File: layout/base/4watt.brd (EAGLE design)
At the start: 50 x 50 mm, 45 parts, among them IC2 FT232RL, Q1 IRF7413, Q2 IRF7413, Q3 IRF7413, Q4 IRF7413, T1 BC848, T2 BC848, T3 BC848, T4 BC848, T5 BC848, T6 BC848, U1 MOD-WIFI-ESP8266-DEV_SMD

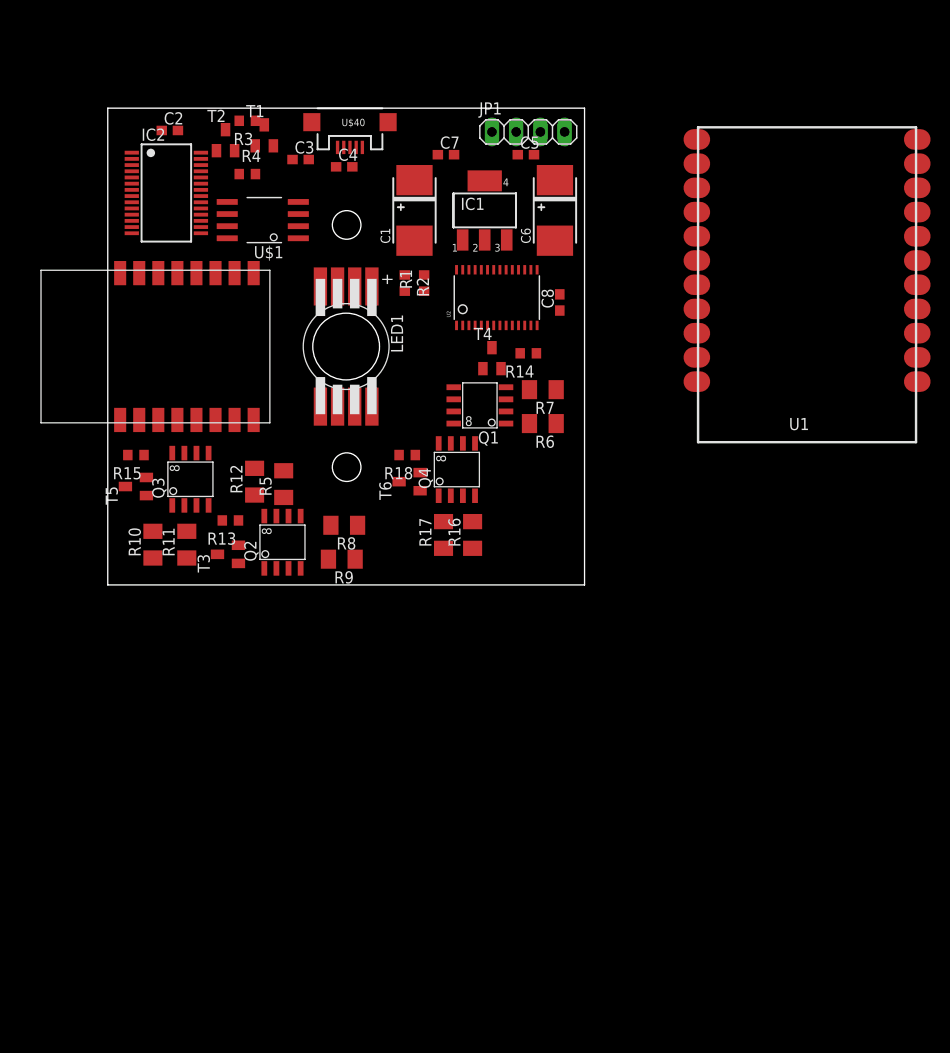
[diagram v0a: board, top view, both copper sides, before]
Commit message: new pinout
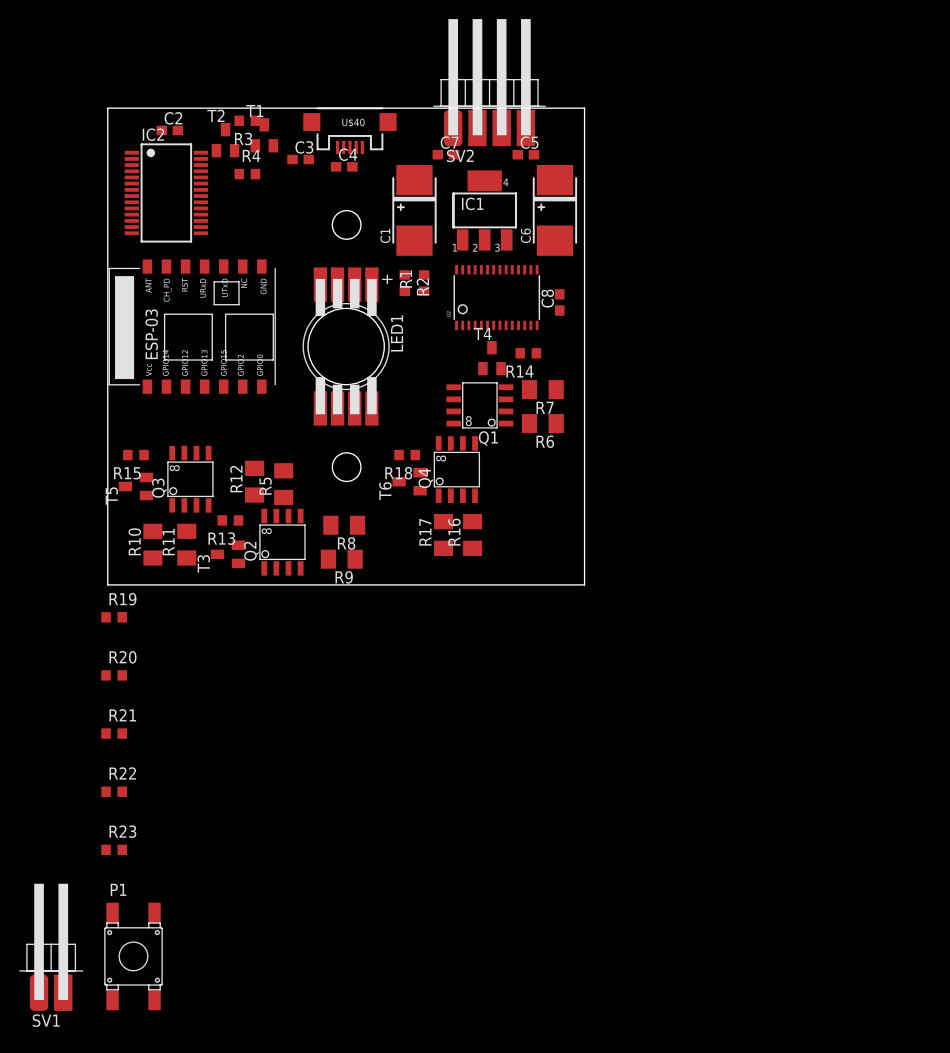
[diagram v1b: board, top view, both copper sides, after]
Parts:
- removed IC3: (no value), ESP8266-2:ESP-12
- removed JP1: (no value), pinhead-2:1X04
- removed U$1: DUMMY, SparkFun:SO08WIDE
- removed U1: MOD-WIFI-ESP8266-DEV_SMD, ESP8266 2:MOD-WIFI-ESP8266-DEV_SMD
- added P1: FSM4JSMA-SMD, switch-misc:FSM4JSMA-SMD
- added R19, R20, R21, R22, R23: 10k, rcl-2:R0603
- added SV1: 1X2SMD-2.54LIEGEND, sid:1X2SMD-2.54LIEGEND
- added SV2: 1X4SMD-2.54LIEGEND, sid:1X4SMD-2.54LIEGEND
- added U$2: ESP8266, ESP8266:ESP-03
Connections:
- removed net GPIO13: U1.18
- removed net VCC: U$1.6
- new net N$2: R19.1, U$2.CH_PD
- new net N$6: R21.1, U$2.GPIO2
- net +3V3: now also R19.2, R20.2, R21.2, R23.2, U$2.VCC; no longer U1.1
- net +5V: now also SV2.P$4
- net GND: now also P1.P$3, P1.P$4, R22.1, SV1.P$1, SV2.P$1, U$2.GND; no longer U$1.7, U1.2
- net GPIO0: now also P1.P$1, P1.P$2, R23.1, SV1.P$2, U$2.GPIO0; no longer U1.21
- net GPIO15: now also R22.2, U$2.GPIO15; no longer U1.19
- net N$3: now also SV2.P$2
- net N$4: now also SV2.P$3
- net RST: now also R20.1, U$2.GPIO18; no longer U1.13
- net RX: now also U$2.URXD
- net SCL: now also U$2.GPIO12; no longer U1.22
- net SDA: now also U$2.NC; no longer U1.11
- net TX: now also U$2.UTXD

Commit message: extclk to gnd
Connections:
- net GND: now also U2.25
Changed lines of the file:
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@@
 <contactref element="SV1" pad="P$1"/>
 <contactref element="SV2" pad="P$1"/>
+<contactref element="U2" pad="25"/>
 <wire x1="46.316" y1="55.118" x2="54.698" y2="55.118" width="0" layer="19" extent="1-1"/>
-<wire x1="39.4" y1="58.532" x2="46.316" y2="55.118" width="0" layer="19" extent="1-1"/>
+<wire x1="46.228" y1="57.912" x2="46.316" y2="55.118" width="0" layer="19" extent="1-1"/>
+<wire x1="39.4" y1="58.532" x2="46.228" y2="57.912" width="0" layer="19" extent="1-1"/>
 <wire x1="34.1" y1="55.882" x2="39.4" y2="58.532" width="0" layer="19" extent="1-1"/>
 <wire x1="35.648" y1="53.848" x2="34.1" y2="55.882" width="0" layer="19" extent="1-1"/>
@@
 <wire x1="31.4" y1="58.532" x2="34.1" y2="55.882" width="0" layer="19" extent="1-1"/>
 <wire x1="47.2191" y1="46.1769" x2="46.316" y2="55.118" width="0" layer="19" extent="1-1"/>
-<wire x1="49.175" y1="43.0498" x2="47.2191" y2="46.1769" width="0" layer="19" extent="1-1"/>
+<wire x1="48.525" y1="43.0498" x2="47.2191" y2="46.1769" width="0" layer="19" extent="1-1"/>
+<wire x1="49.175" y1="43.0498" x2="48.525" y2="43.0498" width="0" layer="19" extent="1-1"/>
 <wire x1="49.825" y1="43.0498" x2="49.175" y2="43.0498" width="0" layer="19" extent="1-1"/>
 <wire x1="42.164" y1="46.101" x2="47.2191" y2="46.1769" width="0" layer="19" extent="1-1"/>
@@
 <wire x1="14.904" y1="-33.556" x2="14.904" y2="-24.372" width="0" layer="19" extent="1-1"/>
 <wire x1="2.794" y1="-32.766" x2="14.904" y2="-33.556" width="0" layer="19" extent="1-1"/>
-<wire x1="46.228" y1="57.912" x2="2.794" y2="-32.766" width="0" layer="19" extent="1-1"/>
 </signal>
 <signal name="N$12">

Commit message: 4watt done
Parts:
- added C9: 100n, rcl:C0603
- R10, R11, R12, R16, R17, R5, R6, R7, R8, R9: value 3,3-3,9 -> 3R6
- R13, R14, R15, R18: value 1k5 -> 360
- moved SV1 100.8 mm to (53.8, 55.1)
- moved P1 85.4 mm to (53.6, 46.0), turned to 180 degrees
- moved R23 72.9 mm to (53.6, 41.1), turned to 90 degrees
- moved R20 48.8 mm to (30.6, 45.1), turned to 270 degrees
- moved C6 46.8 mm to (15.3, 27.7)
- moved R22 44.3 mm to (29.7, 28.3), turned to 180 degrees
- moved R21 40.7 mm to (29.7, 30.3)
- moved R19 25.6 mm to (18.8, 30.8), turned to 270 degrees
- moved C5 20.7 mm to (40.0, 39.8), turned to 270 degrees
- moved C7 16.4 mm to (45.4, 38.8)
- moved C8 15.8 mm to (42.0, 36.2), turned to 270 degrees
- moved R7 15.7 mm to (47.2, 17.2), turned to 90 degrees
- moved R14 15.0 mm to (46.8, 21.2), turned to 270 degrees
- moved T4 12.6 mm to (49.6, 21.2), turned to 90 degrees
- moved C2 12.0 mm to (28.2, 55.1), turned to 90 degrees
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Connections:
- net GND: now also C9.2
- net RST: now also C9.1
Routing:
- net GND: track 0.00 -> 399.0 mm, vias 0 -> 38
- net +3V3: track 0.00 -> 103.3 mm, vias 0 -> 4
- net GPIO0: track 0.00 -> 66.7 mm, vias 0 -> 2
- net +5V: track 0.00 -> 64.8 mm, vias 0 -> 2
- net B: track 0.00 -> 50.8 mm, vias 0 -> 2
- net SCL: track 0.00 -> 41.6 mm, vias 0 -> 2
- net N$4: track 0.00 -> 39.1 mm, vias 0 -> 3
- net R: track 0.00 -> 34.8 mm, vias 0 -> 2
- net SDA: track 0.00 -> 33.4 mm, vias 0 -> 2
- net N$3: track 0.00 -> 31.7 mm, vias 0 -> 3
- net W: track 0.00 -> 24.7 mm, vias 0 -> 2
- net N$1: track 0.00 -> 24.1 mm
- net N$28: track 0.00 -> 22.5 mm
- net RST: track 0.00 -> 19.2 mm, vias 0 -> 2
- net N$31: track 0.00 -> 18.5 mm
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- added copper zone on layer 1, net GND
- added copper zone on layer 16, net GND
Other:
- board size 50 x 50 mm -> 44.5 x 43.2 mm
- board text added: "WiFi Yaala 4W S1D 15"
